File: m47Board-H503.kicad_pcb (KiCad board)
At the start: 2 copper layers, 42 parts, among them J1 USB_C_Receptacle_USB2.0_14P, J3 Conn_01x15_Pin, J4 Conn_01x10_Pin, J5 Conn_01x15_Pin, SW1 SW_Push, SW2 SW_Push, SW3 SW_Push, U1 AP2114H-3.3TRG1, U2 STM32H503CBTx, U3 USBLC6-2SC6, Y1 CX3225FB16000F0FZZH1 16MHz, Y2 ABS07-32.768KHZ-T

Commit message: Update PCB layout
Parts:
- moved C10 34.6 mm to (126.6, 97.6)
- moved SW1 21.3 mm to (131.3, 93.7), turned to 0 degrees
- moved C7 19.2 mm to (153.6, 91.3)
- moved C18 16.7 mm to (127.0, 107.7), turned to 90 degrees
- moved R2 13.6 mm to (149.1, 97.5)
- moved R4 13.4 mm to (150.9, 107.1), turned to -90 degrees
- moved R3 12.4 mm to (150.9, 95.8), turned to 90 degrees
- moved C1 12.0 mm to (146.9, 109.7), turned to -90 degrees
- moved R1 11.4 mm to (145.2, 110.5)
- moved C8 11.1 mm to (149.2, 113.7), turned to 90 degrees
- moved Y1 10.0 mm to (129.6, 105.8)
- moved R9 9.96 mm to (126.0, 107.7), turned to -90 degrees
- moved Y2 9.88 mm to (130.2, 101.2)
- moved C11 9.85 mm to (147.2, 105.2)
- moved C14 9.85 mm to (131.9, 104.7)
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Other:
- board outline added: 40 x 34 mm

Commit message: Update PCB layout
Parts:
- moved C11 0.43 mm to (147.6, 105.2)
- moved C6 0.22 mm to (134.7, 105.5)
- moved C4 0.20 mm to (145.7, 100.0)
- moved Y1 0.16 mm to (129.6, 105.6)
- moved R1 0.12 mm to (145.2, 110.3)
- moved C7 0.12 mm to (153.4, 91.4)
- moved C1 0.11 mm to (146.9, 109.8)
- moved C9 0.11 mm to (149.2, 109.8)
- moved D3 0.11 mm to (141.7, 113.7)
- moved C18 0.10 mm to (127.1, 107.8)
- moved C14 0.10 mm to (131.9, 104.6)
- moved C15 0.10 mm to (131.9, 107.0)
- moved D1 0.08 mm to (146.9, 113.8)
- moved C5 0.06 mm to (138.1, 98.0)
- moved R7 0.06 mm to (127.7, 102.7)
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
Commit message: Update PCB layout, start routing traces
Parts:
- moved R8 2.45 mm to (138.8, 110.3)
- moved D1 1.95 mm to (145.2, 114.7), turned to 180 degrees
- moved D3 1.47 mm to (140.6, 114.7), turned to 180 degrees
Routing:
- net +3.3V: track 0.00 -> 11.7 mm
- net /PC14: track 0.00 -> 9.22 mm
- net /HSE_IN: track 0.00 -> 9.16 mm
- net /PC15: track 0.00 -> 8.95 mm
- net /HSE_OUT: track 0.00 -> 7.24 mm
- net VBUS: track 0.00 -> 5.70 mm
- net GND: track 0.00 -> 5.44 mm
- net Net-(J1-D+-PadA6): track 0.00 -> 3.42 mm
- net Net-(J1-D--PadA7): track 0.00 -> 3.40 mm
- net /USB_D-: track 0.00 -> 2.66 mm
- net /USB_D+: track 0.00 -> 2.63 mm
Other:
- copper layers 2 -> 4
- board text added: "3V3"
- board text added: "USRLED"

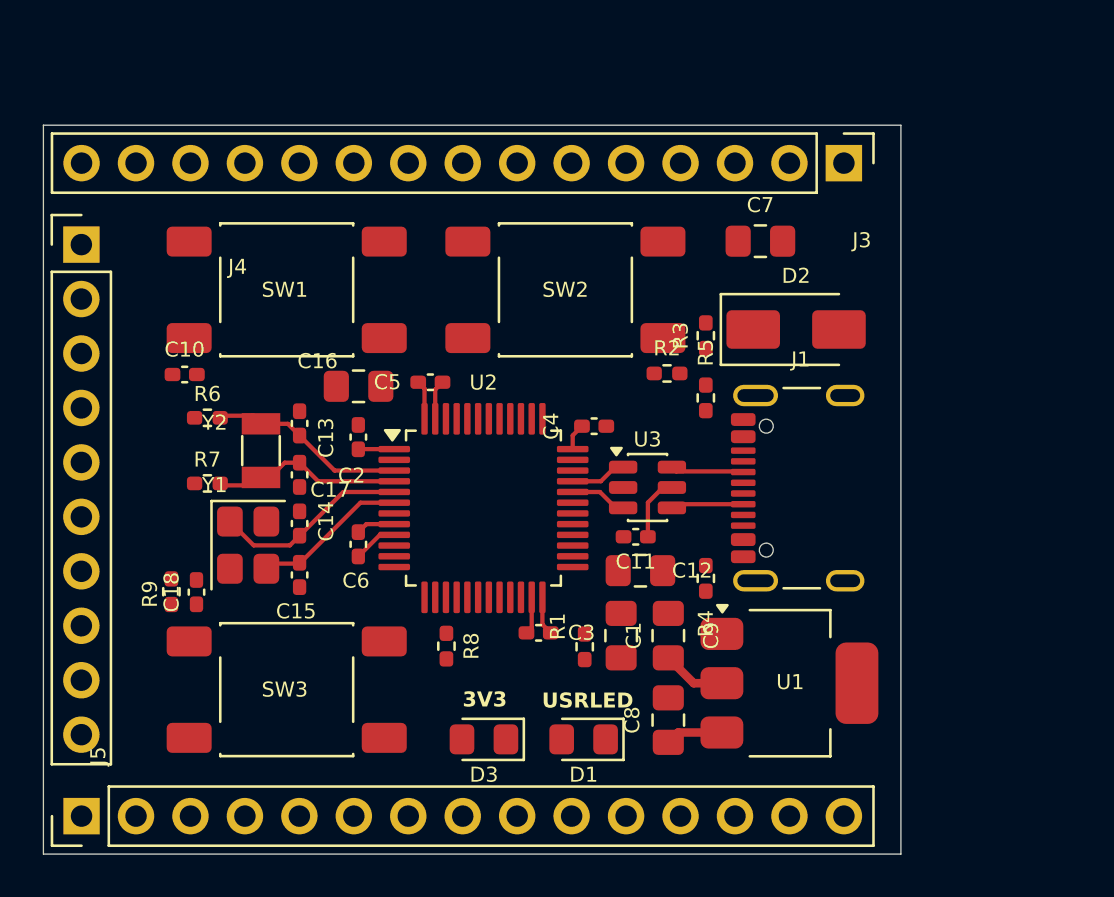
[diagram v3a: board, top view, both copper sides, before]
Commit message: Route some traces, do some silkscreen, change USB-C symbol, change larger caps footprints to 0603
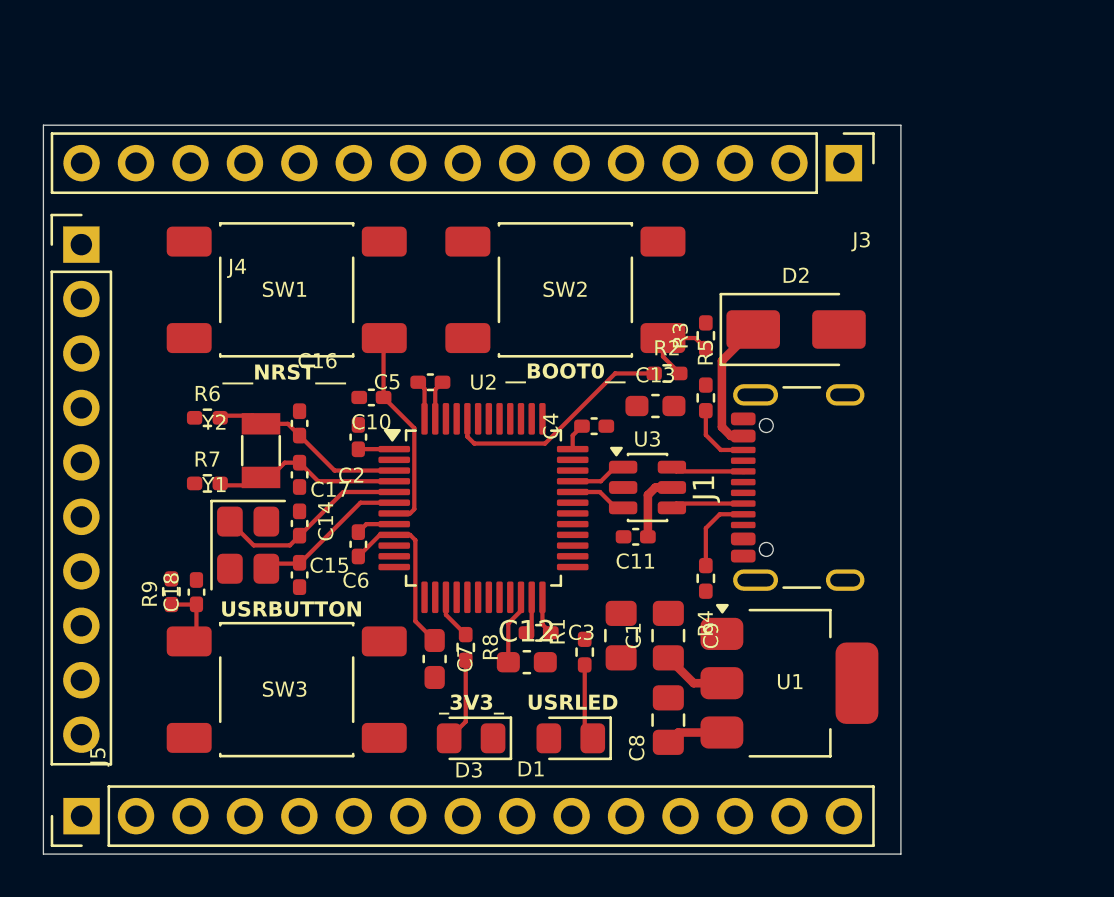
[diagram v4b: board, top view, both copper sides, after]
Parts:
- C12, C13, C7: footprint Capacitor_SMD:C_0805_2012Metric_Pad1.18x1.45mm_HandSolder -> Capacitor_SMD:C_0603_1608Metric_Pad1.08x0.95mm_HandSolder
- J1: value USB_C_Receptacle_USB2.0_14P -> USB_C_Receptacle_USB2.0_16P
- moved C7 24.7 mm to (138.2, 110.9), turned to -90 degrees
- moved C13 13.9 mm to (148.6, 99.1), turned to 0 degrees
- moved C10 8.78 mm to (135.3, 98.7), turned to 180 degrees
- moved C12 6.81 mm to (142.6, 111.0)
- moved R8 0.90 mm to (139.7, 110.4)
- moved D3 0.60 mm to (139.9, 114.6)
- moved D1 0.60 mm to (144.6, 114.6)
- moved R1 0.25 mm to (145.2, 110.6)
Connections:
- J1 pad A8: (no net) -> unconnected-(J1-SBU1-PadA8)
- J1 pad B8: (no net) -> unconnected-(J1-SBU2-PadB8)
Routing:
- net /BOOT0: track 0.00 -> 11.0 mm
- net /NRST: track 0.00 -> 9.61 mm
- net VBUS: track 5.70 -> 12.6 mm
- net +3.3V: track 11.7 -> 17.8 mm
- net Net-(R2-Pad2): track 0.00 -> 4.18 mm
- net Net-(D3-A): track 0.00 -> 3.96 mm
- net /USB-C-CC1: track 0.00 -> 3.76 mm
- net Net-(D1-K): track 0.00 -> 3.58 mm
- net Net-(C12-Pad1): track 0.00 -> 3.27 mm
- net /USB-C-CC2: track 0.00 -> 3.17 mm
- net /PC13: track 0.00 -> 3.04 mm
- net /PA5: track 0.00 -> 2.12 mm
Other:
- board text added: "USRBUTTON"
- board text added: "_3V3_"
- board text added: "__BOOT0__"
- board text added: "___NRST___"
- board text removed: "3V3"

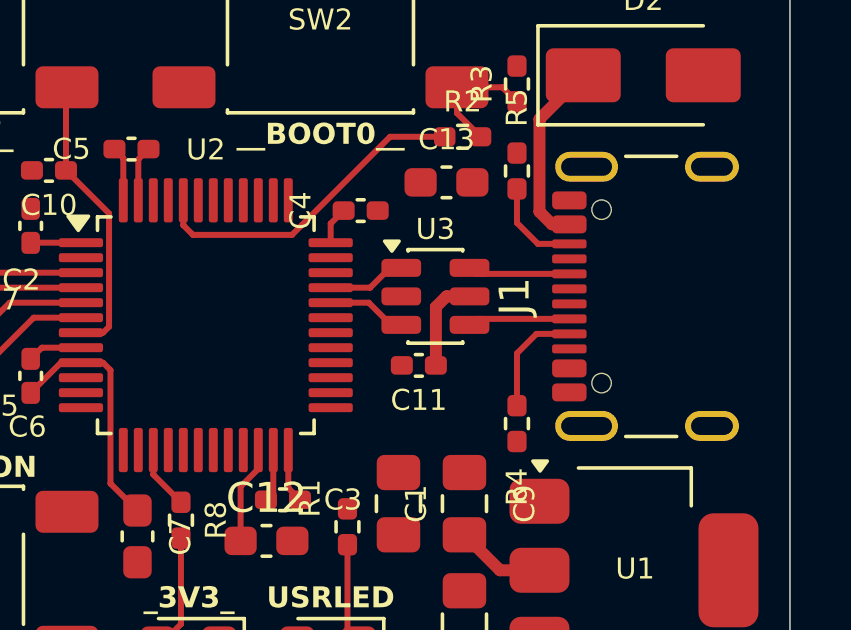
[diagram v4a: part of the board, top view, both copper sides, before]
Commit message: Add net class for usb diff pair
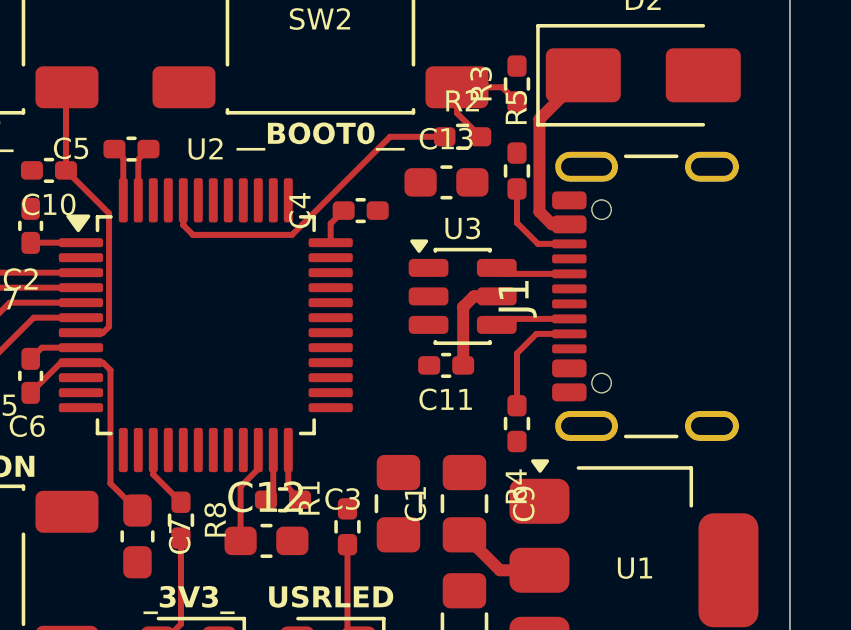
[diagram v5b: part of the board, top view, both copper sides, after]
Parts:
- moved C11 0.91 mm to (148.5, 105.2)
- moved U3 0.91 mm to (149.1, 102.9)
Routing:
- net /USB_D-: track 2.66 -> 0.00 mm
- net /USB_D+: track 2.63 -> 0.00 mm
- net Net-(J1-D--PadA7): track 3.41 -> 2.50 mm
- net Net-(J1-D+-PadA6): track 3.47 -> 2.56 mm
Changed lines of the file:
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@@
 	(footprint "Package_TO_SOT_SMD:SOT-23-6"
 		(layer "F.Cu")
-		(at 148.18 102.9)
+		(at 149.09 102.9)
 		(descr "SOT, 6 Pin (JEDEC MO-178 Var AB https://www.jedec.org/document_search?search_api_views_fulltext=MO-178)")
 		(tags "SOT TO_SOT_SMD")
@@
 	(footprint "Capacitor_SMD:C_0402_1005Metric_Pad0.74x0.62mm_HandSolder"
 		(layer "F.Cu")
-		(at 147.63 105.2 180)
+		(at 148.54 105.2 180)
 		(descr "Capacitor SMD 0402 (1005 Metric), square (rectangular) end terminal, IPC-7351 nominal with elongated pad for handsoldering. (Body size source: IPC-SM-782 page 76, https://www.pcb-3d.com/wordpress/wp-content/uploads/ipc-sm-782a_amendment_1_and_2.pdf)")
 		(tags "capacitor handsolder")
@@
 	)
 	(segment
-		(start 148.55 102.9)
-		(end 149.3175 102.9)
+		(start 149.46 102.9)
+		(end 150.2275 102.9)
 		(width 0.4)
 		(layer "F.Cu")
@@
 	)
 	(segment
-		(start 148.1975 105.2)
-		(end 148.1975 103.2525)
+		(start 149.1075 105.2)
+		(end 149.1075 103.2525)
 		(width 0.4)
 		(layer "F.Cu")
@@
 	)
 	(segment
-		(start 148.9 102.9)
-		(end 149.3175 102.9)
+		(start 149.81 102.91)
+		(end 150.2275 102.91)
 		(width 0.2)
 		(layer "F.Cu")
@@
 	)
 	(segment
-		(start 148.1975 103.2525)
-		(end 148.55 102.9)
+		(start 149.1075 103.2525)
+		(end 149.46 102.9)
 		(width 0.4)
 		(layer "F.Cu")
@@
 	)
 	(segment
-		(start 146.005039 102.61)
-		(end 146.665039 101.95)
+		(start 152.645 103.65)
+		(end 150.4275 103.65)
 		(width 0.2)
 		(layer "F.Cu")
-		(net "/USB_D+")
-	)
-	(segment
-		(start 146.665039 101.95)
-		(end 147.0425 101.95)
-		(width 0.2)
-		(layer "F.Cu")
-		(net "/USB_D+")
+		(net "Net-(J1-D--PadA7)")
 	)
 	(segment
-		(start 144.69 102.61)
-		(end 146.005039 102.61)
+		(start 150.4275 103.65)
+		(end 150.2275 103.85)
 		(width 0.2)
 		(layer "F.Cu")
-		(net "/USB_D+")
+		(net "Net-(J1-D--PadA7)")
 	)
 	(segment
-		(start 144.69 103.11)
-		(end 145.96 103.11)
+		(start 150.4275 102.15)
+		(end 150.2275 101.95)
 		(width 0.2)
 		(layer "F.Cu")
-		(net "/USB_D-")
+		(net "Net-(J1-D+-PadA6)")
 	)
 	(segment
-		(start 145.96 103.11)
-		(end 146.7 103.85)
+		(start 152.6 102.14)
+		(end 152.645 102.185)
 		(width 0.2)
 		(layer "F.Cu")
-		(net "/USB_D-")
+		(net "Net-(J1-D+-PadA6)")
 	)
 	(segment
-		(start 146.7 103.85)
-		(end 147.0425 103.85)
+		(start 152.645 102.15)
+		(end 150.4275 102.15)
 		(width 0.2)
 		(layer "F.Cu")
-		(net "/USB_D-")
+		(net "Net-(J1-D+-PadA6)")
 	)
 	(segment
@@
 		(net "/BOOT0")
 	)
-	(segment
-		(start 152.6 102.14)
-		(end 152.645 102.185)
-		(width 0.2)
-		(layer "F.Cu")
-		(net "Net-(J1-D+-PadA6)")
-	)
-	(segment
-		(start 149.5175 102.15)
-		(end 152.645 102.15)
-		(width 0.2)
-		(layer "F.Cu")
-		(net "Net-(J1-D+-PadA6)")
-	)
-	(segment
-		(start 149.3175 101.95)
-		(end 149.5175 102.15)
-		(width 0.2)
-		(layer "F.Cu")
-		(net "Net-(J1-D+-PadA6)")
-	)
-	(segment
-		(start 149.5175 103.65)
-		(end 152.645 103.65)
-		(width 0.2)
-		(layer "F.Cu")
-		(net "Net-(J1-D--PadA7)")
-	)
-	(segment
-		(start 149.3175 103.85)
-		(end 149.5175 103.65)
-		(width 0.2)
-		(layer "F.Cu")
-		(net "Net-(J1-D--PadA7)")
-	)
 	(embedded_fonts no)

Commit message: Route USB diff pair
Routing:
- net VBUS: track 12.6 -> 6.32 mm
- net +3.3V: track 17.8 -> 24.1 mm
- net /USB_D-: track 0.00 -> 3.56 mm
- net /USB_D+: track 0.00 -> 3.56 mm
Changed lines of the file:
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@@
 		(capping no)
 		(filling no)
+		(zone_defaults)
 		(pcbplotparams
 			(layerselection 0x00000000_00000000_55555555_5755f5ff)
@@
 	(footprint "Resistor_SMD:R_0402_1005Metric_Pad0.72x0.64mm_HandSolder"
 		(layer "F.Cu")
-		(at 150.9 107.14 -90)
+		(at 150.9 107.1 -90)
 		(descr "Resistor SMD 0402 (1005 Metric), square (rectangular) end terminal, IPC-7351 nominal with elongated pad for handsoldering. (Body size source: IPC-SM-782 page 72, https://www.pcb-3d.com/wordpress/wp-content/uploads/ipc-sm-782a_amendment_1_and_2.pdf)")
 		(tags "resistor handsolder")
@@
 	(footprint "Resistor_SMD:R_0402_1005Metric_Pad0.72x0.64mm_HandSolder"
 		(layer "F.Cu")
-		(at 150.9 98.72 90)
+		(at 150.9 98.68 90)
 		(descr "Resistor SMD 0402 (1005 Metric), square (rectangular) end terminal, IPC-7351 nominal with elongated pad for handsoldering. (Body size source: IPC-SM-782 page 72, https://www.pcb-3d.com/wordpress/wp-content/uploads/ipc-sm-782a_amendment_1_and_2.pdf)")
 		(tags "resistor handsolder")
@@
 	(footprint "Package_TO_SOT_SMD:SOT-23-6"
 		(layer "F.Cu")
-		(at 149.09 102.9)
+		(at 149.09 102.86)
 		(descr "SOT, 6 Pin (JEDEC MO-178 Var AB https://www.jedec.org/document_search?search_api_views_fulltext=MO-178)")
 		(tags "SOT TO_SOT_SMD")
@@
 	(footprint "Connector_USB:USB_C_Receptacle_GCT_USB4105-xx-A_16P_TopMnt_Horizontal"
 		(layer "F.Cu")
-		(at 156.325 102.9 90)
+		(at 156.325 102.86 90)
 		(descr "USB 2.0 Type C Receptacle, GCT, 16P, top mounted, horizontal, 5A: https://gct.co/files/drawings/usb4105.pdf")
 		(tags "USB C Type-C Receptacle SMD USB 2.0 16P 16C USB4105-15-A USB4105-15-A-060 USB4105-15-A-120 USB4105-GF-A USB4105-GF-A-060 USB4105-GF-A-120")
@@
 	(footprint "Capacitor_SMD:C_0402_1005Metric_Pad0.74x0.62mm_HandSolder"
 		(layer "F.Cu")
-		(at 148.54 105.2 180)
+		(at 148.54 105.16 180)
 		(descr "Capacitor SMD 0402 (1005 Metric), square (rectangular) end terminal, IPC-7351 nominal with elongated pad for handsoldering. (Body size source: IPC-SM-782 page 76, https://www.pcb-3d.com/wordpress/wp-content/uploads/ipc-sm-782a_amendment_1_and_2.pdf)")
 		(tags "capacitor handsolder")
@@
 	)
 	(segment
-		(start 151.55 104.15)
-		(end 152.645 104.15)
-		(width 0.2)
+		(start 150.9 105.09)
+		(end 150.9 106.5025)
+		(width 0.3)
 		(layer "F.Cu")
 		(net "/USB-C-CC1")
 	)
 	(segment
-		(start 150.9 106.5425)
-		(end 150.9 104.8)
-		(width 0.2)
+		(start 152.645 104.11)
+		(end 151.88 104.11)
+		(width 0.3)
 		(layer "F.Cu")
 		(net "/USB-C-CC1")
 	)
 	(segment
-		(start 150.9 104.8)
-		(end 151.55 104.15)
-		(width 0.2)
+		(start 151.88 104.11)
+		(end 150.9 105.09)
+		(width 0.3)
 		(layer "F.Cu")
 		(net "/USB-C-CC1")
@@
 	)
 	(segment
-		(start 149.46 102.9)
-		(end 150.2275 102.9)
+		(start 149.46 102.86)
+		(end 150.2275 102.86)
 		(width 0.4)
 		(layer "F.Cu")
@@
 	)
 	(segment
-		(start 151.65 100.079999)
-		(end 152.070001 100.5)
+		(start 149.1075 105.16)
+		(end 149.1075 103.2125)
 		(width 0.4)
 		(layer "F.Cu")
@@
 	)
 	(segment
-		(start 149.1075 105.2)
-		(end 149.1075 103.2525)
-		(width 0.4)
-		(layer "F.Cu")
-		(net "VBUS")
-	)
-	(segment
-		(start 149.81 102.91)
-		(end 150.2275 102.91)
+		(start 149.81 102.87)
+		(end 150.2275 102.87)
 		(width 0.2)
 		(layer "F.Cu")
@@
 	)
 	(segment
-		(start 153.11 95.53)
-		(end 151.65 96.99)
-		(width 0.4)
-		(layer "F.Cu")
-		(net "VBUS")
-	)
-	(segment
-		(start 152.070001 100.5)
-		(end 152.645 100.5)
-		(width 0.4)
-		(layer "F.Cu")
-		(net "VBUS")
-	)
-	(segment
-		(start 151.65 96.99)
-		(end 151.65 100.079999)
-		(width 0.4)
-		(layer "F.Cu")
-		(net "VBUS")
-	)
-	(segment
 		(start 151.65 114.33)
 		(end 149.6075 114.33)
@@
 	)
 	(segment
-		(start 149.1075 103.2525)
-		(end 149.46 102.9)
+		(start 149.1075 103.2125)
+		(end 149.46 102.86)
 		(width 0.4)
 		(layer "F.Cu")
@@
 	)
 	(segment
+		(start 157.95 112.03)
+		(end 151.65 112.03)
+		(width 0.4)
+		(layer "F.Cu")
+		(net "+3.3V")
+	)
+	(segment
 		(start 151.65 112.03)
 		(end 150.3325 112.03)
@@
 	)
 	(segment
-		(start 150.9 99.3175)
-		(end 150.9 100.45)
-		(width 0.2)
+		(start 151.885 101.11)
+		(end 150.9 100.125)
+		(width 0.3)
 		(layer "F.Cu")
 		(net "/USB-C-CC2")
 	)
 	(segment
-		(start 150.9 100.45)
-		(end 151.6 101.15)
-		(width 0.2)
+		(start 152.645 101.11)
+		(end 151.885 101.11)
+		(width 0.3)
 		(layer "F.Cu")
 		(net "/USB-C-CC2")
 	)
 	(segment
-		(start 151.6 101.15)
-		(end 152.645 101.15)
-		(width 0.2)
+		(start 150.9 100.125)
+		(end 150.9 99.2775)
+		(width 0.3)
 		(layer "F.Cu")
 		(net "/USB-C-CC2")
@@
 	)
 	(segment
-		(start 152.645 103.65)
-		(end 150.4275 103.65)
-		(width 0.2)
+		(start 144.69 102.61)
+		(end 145.2775 102.61)
+		(width 0.32)
+		(layer "F.Cu")
+		(net "/USB_D+")
+	)
+	(segment
+		(start 145.2925 102.625)
+		(end 146.875 102.625)
+		(width 0.32)
+		(layer "F.Cu")
+		(net "/USB_D+")
+	)
+	(segment
+		(start 147.59 101.91)
+		(end 147.9525 101.91)
+		(width 0.32)
+		(layer "F.Cu")
+		(net "/USB_D+")
+	)
+	(segment
+		(start 146.875 102.625)
+		(end 147.59 101.91)
+		(width 0.32)
+		(layer "F.Cu")
+		(net "/USB_D+")
+	)
+	(segment
+		(start 145.2775 102.61)
+		(end 145.2925 102.625)
+		(width 0.32)
+		(layer "F.Cu")
+		(net "/USB_D+")
+	)
+	(segment
+		(start 145.2925 103.095)
+		(end 146.875 103.095)
+		(width 0.32)
+		(layer "F.Cu")
+		(net "/USB_D-")
+	)
+	(segment
+		(start 147.59 103.81)
+		(end 147.9525 103.81)
+		(width 0.32)
+		(layer "F.Cu")
+		(net "/USB_D-")
+	)
+	(segment
+		(start 145.2775 103.11)
+		(end 145.2925 103.095)
+		(width 0.32)
+		(layer "F.Cu")
+		(net "/USB_D-")
+	)
+	(segment
+		(start 144.69 103.11)
+		(end 145.2775 103.11)
+		(width 0.32)
+		(layer "F.Cu")
+		(net "/USB_D-")
+	)
+	(segment
+		(start 146.875 103.095)
+		(end 147.59 103.81)
+		(width 0.32)
+		(layer "F.Cu")
+		(net "/USB_D-")
+	)
+	(segment
+		(start 152.645 103.61)
+		(end 150.4275 103.61)
+		(width 0.3)
 		(layer "F.Cu")
 		(net "Net-(J1-D--PadA7)")
 	)
 	(segment
-		(start 150.4275 103.65)
-		(end 150.2275 103.85)
-		(width 0.2)
+		(start 150.4275 103.61)
+		(end 150.2275 103.81)
+		(width 0.3)
 		(layer "F.Cu")
 		(net "Net-(J1-D--PadA7)")
 	)
 	(segment
-		(start 150.4275 102.15)
-		(end 150.2275 101.95)
+		(start 152.6 102.1)
+		(end 152.645 102.145)
 		(width 0.2)
 		(layer "F.Cu")
@@
 	)
 	(segment
-		(start 152.6 102.14)
-		(end 152.645 102.185)
-		(width 0.2)
+		(start 150.4275 102.11)
+		(end 150.2275 101.91)
+		(width 0.3)
 		(layer "F.Cu")
 		(net "Net-(J1-D+-PadA6)")
 	)
 	(segment
-		(start 152.645 102.15)
-		(end 150.4275 102.15)
-		(width 0.2)
+		(start 152.645 102.11)
+		(end 150.4275 102.11)
+		(width 0.3)
 		(layer "F.Cu")
 		(net "Net-(J1-D+-PadA6)")
